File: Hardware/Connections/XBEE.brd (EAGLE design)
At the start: 34.3 x 28.9 mm, 3 parts

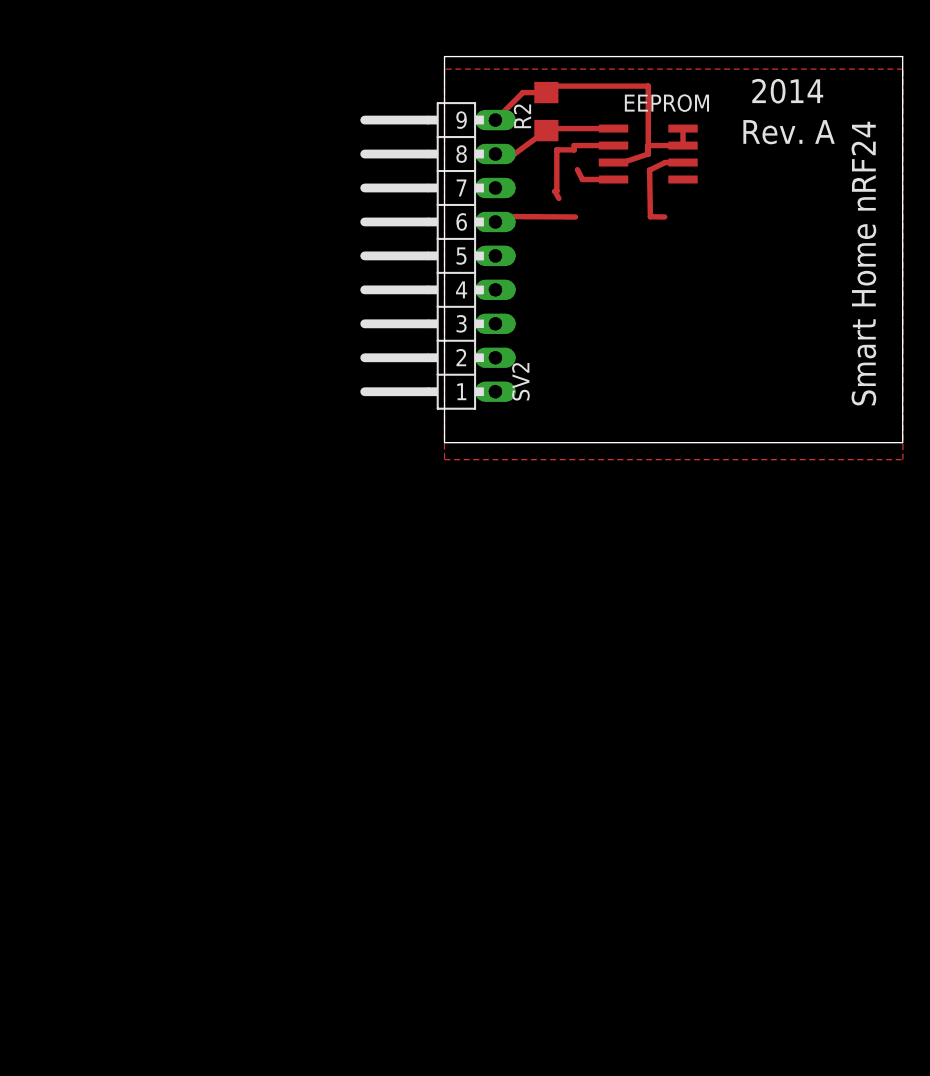
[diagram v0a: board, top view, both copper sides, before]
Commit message: updated XBEE Schematic. Added 3 Extra Pins for Serial protocol
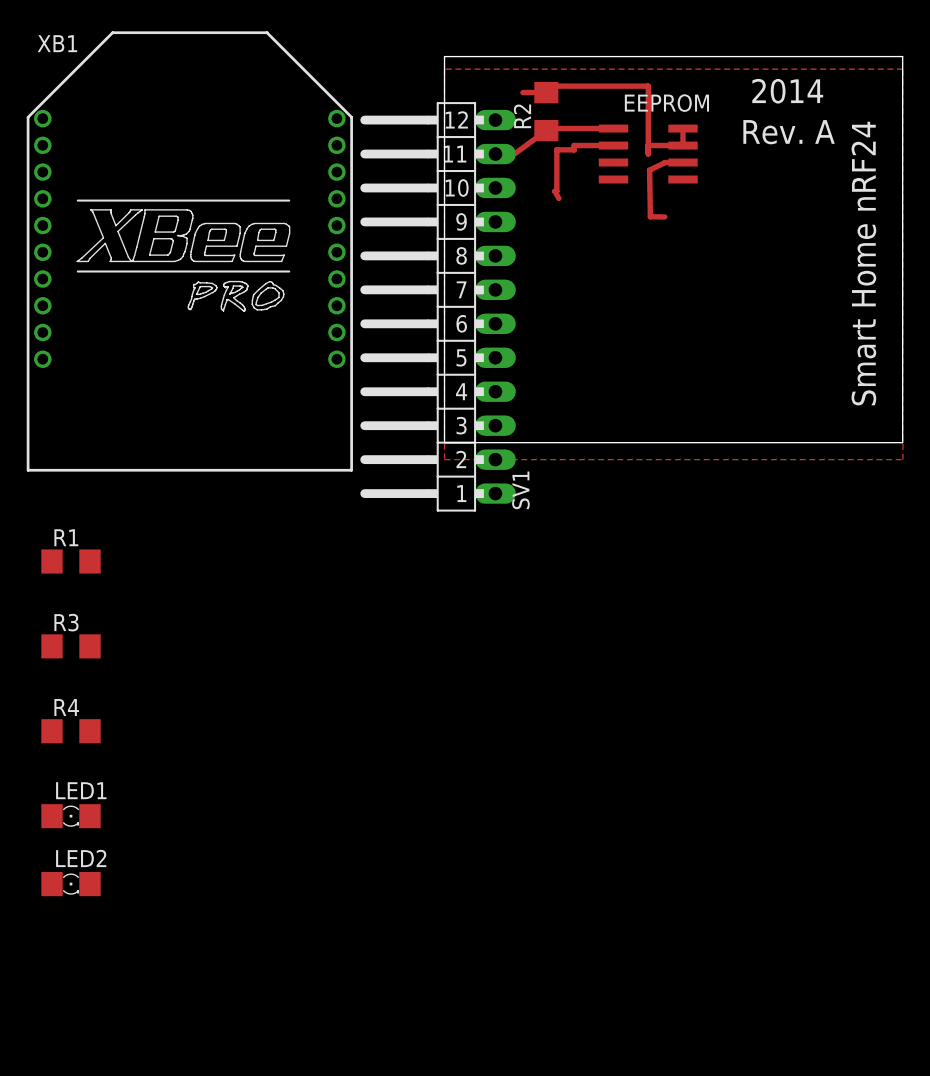
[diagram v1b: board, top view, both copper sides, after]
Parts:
- removed SV2: CON1, con-lstb:MA09-1W
- added LED1: ON_SLEEP, led:1206
- added LED2: Assoc, led:1206
- added R1, R3, R4: 10K, resistor:R1206
- added SV1: CON1, con-lstb:MA12-1W
- added XB1: XBEE-PRO, maxstream:XBEE-PRO
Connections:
- removed net N$4: EEPROM.4
- new net N$1: R1.2, XB1.5
- new net N$3: R4.2, XB1.13
- new net N$5: R3.2, XB1.15
- new net N$6: LED1.A, R4.1
- new net N$7: LED2.A, R3.1
- new net UART_RX: SV1.3, XB1.3
- new net UART_TX: SV1.2, XB1.2
- net +3V3: now also R1.1, SV1.12, XB1.1; no longer SV2.9
- net CE_RAD: now also SV1.5; no longer SV2.2
- net CSN_MEM: now also SV1.11; no longer SV2.8
- net CSN_RAD: now also SV1.6; no longer SV2.3
- net GND: now also EEPROM.4, LED1.C, LED2.C, SV1.4, XB1.10, XB1.14; no longer SV2.1
- net IRQ_RAD: now also SV1.8; no longer SV2.5
- net MISO: now also SV1.10; no longer SV2.7
- net MOSI: now also SV1.7; no longer SV2.4
- net SCK: now also SV1.9; no longer SV2.6
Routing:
- net SCK: track 13.2 -> 7.19 mm
- net +3V3: track 24.8 -> 19.2 mm
- net N$4: track 3.15 -> 0.00 mm
- net CSN_MEM: track 9.42 -> 8.00 mm
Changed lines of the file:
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@@
 </autorouter>
 <elements>
-<element name="SV2" library="con-lstb" package="MA09-1W" value="CON1" x="3.81" y="13.97" rot="R90">
-<attribute name="OC_NEWARK" value="unknown" x="25.4" y="39.37" size="1.778" layer="27" rot="R90" display="off"/>
-<attribute name="MPN" value="" x="25.4" y="39.37" size="1.778" layer="27" rot="R90" display="off"/>
-<attribute name="MF" value="" x="25.4" y="39.37" size="1.778" layer="27" rot="R90" display="off"/>
-<attribute name="OC_FARNELL" value="unknown" x="25.4" y="39.37" size="1.778" layer="27" rot="R90" display="off"/>
-</element>
 <element name="EEPROM" library="eeprom" package="SO8" value="BR25S640FJ-WE2" x="15.24" y="21.59" rot="R270"/>
 <element name="R2" library="resistor" package="R1206" value="10K" x="7.62" y="24.765" rot="R90"/>
+<element name="SV1" library="con-lstb" package="MA12-1W" value="CON1" x="3.81" y="10.16" rot="R90">
+<attribute name="OC_NEWARK" value="unknown" x="3.81" y="10.16" size="1.778" layer="27" rot="R90" display="off"/>
+<attribute name="MPN" value="" x="3.81" y="10.16" size="1.778" layer="27" rot="R90" display="off"/>
+<attribute name="MF" value="" x="3.81" y="10.16" size="1.778" layer="27" rot="R90" display="off"/>
+<attribute name="OC_FARNELL" value="unknown" x="3.81" y="10.16" size="1.778" layer="27" rot="R90" display="off"/>
+</element>
+<element name="XB1" library="maxstream" package="XBEE-PRO" value="XBEE-PRO" x="-19.05" y="15.24">
+<attribute name="OC_NEWARK" value="42M2667" x="-19.05" y="15.24" size="1.778" layer="27" display="off"/>
+<attribute name="MPN" value="XBP24-AWI-001" x="-19.05" y="15.24" size="1.778" layer="27" display="off"/>
+<attribute name="MF" value="" x="-19.05" y="15.24" size="1.778" layer="27" display="off"/>
+<attribute name="OC_FARNELL" value="1337916" x="-19.05" y="15.24" size="1.778" layer="27" display="off"/>
+</element>
+<element name="R1" library="resistor" package="R1206" value="10K" x="-27.94" y="-8.89"/>
+<element name="R3" library="resistor" package="R1206" value="10K" x="-27.94" y="-15.24"/>
+<element name="R4" library="resistor" package="R1206" value="10K" x="-27.94" y="-21.59"/>
+<element name="LED1" library="led" package="1206" value="ON_SLEEP" x="-27.94" y="-27.94"/>
+<element name="LED2" library="led" package="1206" value="Assoc" x="-27.94" y="-33.02"/>
 </elements>
 <signals>
 <signal name="+3V3">
-<contactref element="SV2" pad="9"/>
 <contactref element="EEPROM" pad="8"/>
 <contactref element="EEPROM" pad="7"/>
-<contactref element="EEPROM" pad="3"/>
 <contactref element="R2" pad="2"/>
 <wire x1="17.84" y1="23.495" x2="17.84" y2="22.225" width="0.4064" layer="1"/>
 <wire x1="7.62" y1="26.187" x2="5.867" y2="26.187" width="0.4064" layer="1"/>
-<wire x1="5.867" y1="26.187" x2="3.81" y2="24.13" width="0.4064" layer="1"/>
 <wire x1="17.84" y1="22.225" x2="15.205" y2="22.225" width="0.4064" layer="1"/>
 <wire x1="15.205" y1="22.225" x2="15.24" y2="21.59" width="0.4064" layer="1"/>
-<wire x1="15.24" y1="21.59" x2="13.335" y2="20.955" width="0.4064" layer="1"/>
-<wire x1="13.335" y1="20.955" x2="12.64" y2="20.955" width="0.4064" layer="1"/>
 <wire x1="7.62" y1="26.187" x2="8.103" y2="26.67" width="0.4064" layer="1"/>
 <wire x1="8.103" y1="26.67" x2="15.24" y2="26.67" width="0.4064" layer="1"/>
 <wire x1="15.24" y1="26.67" x2="15.24" y2="21.59" width="0.4064" layer="1"/>
+<contactref element="EEPROM" pad="3"/>
+<contactref element="SV1" pad="12"/>
+<contactref element="XB1" pad="1"/>
+<contactref element="R1" pad="1"/>
+<wire x1="-30.05" y1="24.24" x2="-29.362" y2="-8.89" width="0" layer="19" extent="1-1"/>
+<wire x1="3.81" y1="24.13" x2="-30.05" y2="24.24" width="0" layer="19" extent="1-1"/>
+<wire x1="5.867" y1="26.187" x2="3.81" y2="24.13" width="0" layer="19" extent="1-1"/>
+<wire x1="12.64" y1="20.955" x2="15.24" y2="21.59" width="0" layer="19" extent="1-1"/>
 </signal>
 <signal name="GND">
-<contactref element="SV2" pad="1"/>
 <polygon width="0.4064" layer="1" isolate="0.4064">
 <vertex x="0" y="27.94"/>
@@
 <vertex x="34.29" y="27.94"/>
 </polygon>
+<contactref element="EEPROM" pad="4"/>
+<contactref element="SV1" pad="4"/>
+<contactref element="XB1" pad="10"/>
+<contactref element="XB1" pad="10"/>
+<contactref element="XB1" pad="14"/>
+<contactref element="LED2" pad="C"/>
+<contactref element="LED1" pad="C"/>
+<wire x1="-26.518" y1="-27.94" x2="-26.518" y2="-33.02" width="0" layer="19" extent="1-1"/>
+<wire x1="-30.05" y1="6.24" x2="-26.518" y2="-27.94" width="0" layer="19" extent="1-1"/>
+<wire x1="-8.05" y1="12.24" x2="-30.05" y2="6.24" width="0" layer="19" extent="1-1"/>
+<wire x1="3.81" y1="3.81" x2="-8.05" y2="12.24" width="0" layer="19" extent="1-1"/>
+<wire x1="12.64" y1="19.685" x2="3.81" y2="3.81" width="0" layer="19" extent="1-1"/>
 </signal>
 <signal name="MISO">
 <contactref element="EEPROM" pad="2"/>
-<contactref element="SV2" pad="7"/>
 <wire x1="12.64" y1="22.225" x2="9.7" y2="22.225" width="0.4064" layer="1"/>
 <wire x1="9.7" y1="22.225" x2="9.7" y2="21.9" width="0.4064" layer="1"/>
@@
 <wire x1="8.4" y1="18.8" x2="8.255" y2="18.8" width="0.4064" layer="1"/>
 <wire x1="8.255" y1="18.8" x2="8.555" y2="18.267" width="0.4064" layer="1"/>
-<wire x1="3.81" y1="18.8" x2="3.81" y2="19.05" width="0.4064" layer="1"/>
+<contactref element="SV1" pad="10"/>
 <wire x1="3.81" y1="19.05" x2="8.255" y2="18.8" width="0" layer="19" extent="1-1"/>
 </signal>
 <signal name="MOSI">
 <contactref element="EEPROM" pad="5"/>
-<contactref element="SV2" pad="4"/>
+<contactref element="SV1" pad="7"/>
 <wire x1="3.81" y1="11.43" x2="17.84" y2="19.685" width="0" layer="19" extent="1-1"/>
 </signal>
@@
 <wire x1="15.34" y1="20.385" x2="16.51" y2="20.955" width="0.4064" layer="1"/>
 <wire x1="16.51" y1="20.955" x2="17.84" y2="20.955" width="0.4064" layer="1"/>
-<wire x1="9.79" y1="16.88" x2="5.12" y2="16.91" width="0.4064" layer="1"/>
-<contactref element="SV2" pad="6"/>
-<wire x1="5.12" y1="16.91" x2="3.81" y2="16.51" width="0.4064" layer="1"/>
-<wire x1="9.79" y1="16.88" x2="15.4" y2="16.9" width="0" layer="19" extent="1-1"/>
-</signal>
-<signal name="CSN_RAD">
-<contactref element="SV2" pad="3"/>
-</signal>
-<signal name="CE_RAD">
-<contactref element="SV2" pad="2"/>
+<contactref element="SV1" pad="9"/>
+<wire x1="3.81" y1="16.51" x2="15.4" y2="16.9" width="0" layer="19" extent="1-1"/>
 </signal>
 <signal name="CSN_MEM">
 <contactref element="R2" pad="1"/>
 <contactref element="EEPROM" pad="1"/>
-<contactref element="SV2" pad="8"/>
 <wire x1="12.64" y1="23.495" x2="8.407" y2="23.495" width="0.4064" layer="1"/>
 <wire x1="8.407" y1="23.495" x2="7.62" y2="23.343" width="0.4064" layer="1"/>
 <wire x1="7.62" y1="23.343" x2="5.232" y2="21.59" width="0.4064" layer="1"/>
-<wire x1="5.232" y1="21.59" x2="3.81" y2="21.59" width="0.4064" layer="1"/>
-</signal>
-<signal name="IRQ_RAD">
-<contactref element="SV2" pad="5"/>
+<contactref element="SV1" pad="11"/>
+<wire x1="3.81" y1="21.59" x2="5.232" y2="21.59" width="0" layer="19" extent="1-1"/>
 </signal>
 <signal name="N$2">
 </signal>
 <signal name="N$4">
-<contactref element="EEPROM" pad="4"/>
-<wire x1="12.64" y1="19.685" x2="10.312" y2="19.685" width="0.4064" layer="1"/>
-<wire x1="10.312" y1="19.685" x2="9.942" y2="20.42" width="0.4064" layer="1"/>
+</signal>
+<signal name="CSN_RAD">
+<contactref element="SV1" pad="6"/>
+</signal>
+<signal name="CE_RAD">
+<contactref element="SV1" pad="5"/>
+</signal>
+<signal name="IRQ_RAD">
+<contactref element="SV1" pad="8"/>
+</signal>
+<signal name="UART_RX">
+<contactref element="SV1" pad="3"/>
+<contactref element="XB1" pad="3"/>
+<wire x1="3.81" y1="1.27" x2="-30.05" y2="20.24" width="0" layer="19" extent="1-1"/>
+</signal>
+<signal name="UART_TX">
+<contactref element="SV1" pad="2"/>
+<contactref element="XB1" pad="2"/>
+<wire x1="3.81" y1="-1.27" x2="-30.05" y2="22.24" width="0" layer="19" extent="1-1"/>
+</signal>
+<signal name="N$1">
+<contactref element="XB1" pad="5"/>
+<contactref element="R1" pad="2"/>
+<wire x1="-30.05" y1="16.24" x2="-26.518" y2="-8.89" width="0" layer="19" extent="1-1"/>
+</signal>
+<signal name="N$3">
+<contactref element="XB1" pad="13"/>
+<contactref element="R4" pad="2"/>
+<wire x1="-8.05" y1="10.24" x2="-26.518" y2="-21.59" width="0" layer="19" extent="1-1"/>
+</signal>
+<signal name="N$5">
+<contactref element="XB1" pad="15"/>
+<contactref element="R3" pad="2"/>
+<wire x1="-8.05" y1="14.24" x2="-26.518" y2="-15.24" width="0" layer="19" extent="1-1"/>
+</signal>
+<signal name="N$6">
+<contactref element="R4" pad="1"/>
+<contactref element="LED1" pad="A"/>
+<wire x1="-29.362" y1="-21.59" x2="-29.362" y2="-27.94" width="0" layer="19" extent="1-1"/>
+</signal>
+<signal name="N$7">
+<contactref element="R3" pad="1"/>
+<contactref element="LED2" pad="A"/>
+<wire x1="-29.362" y1="-15.24" x2="-29.362" y2="-33.02" width="0" layer="19" extent="1-1"/>
 </signal>
 </signals>

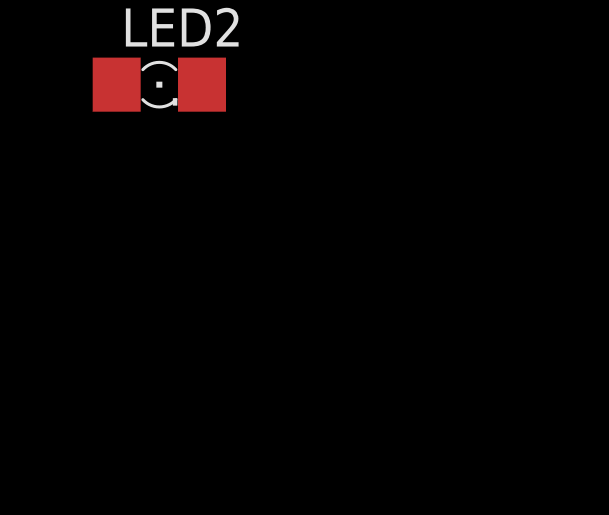
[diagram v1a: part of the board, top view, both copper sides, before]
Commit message: added missing components to XBEE schematic
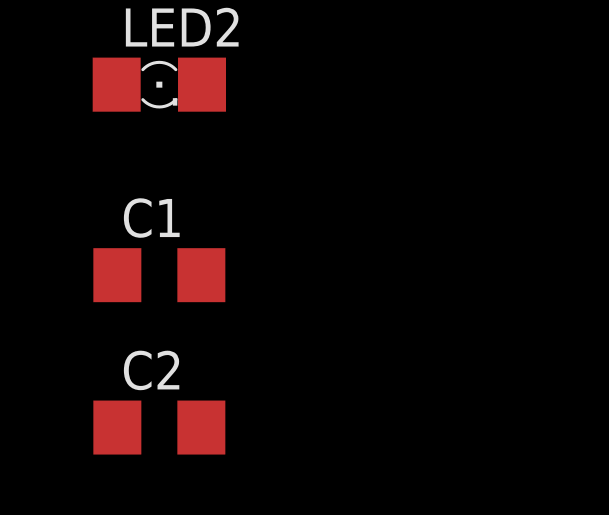
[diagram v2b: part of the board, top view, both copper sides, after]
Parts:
- added C1: 8.2p, rcl:C1206
- added C2: 1u, rcl:C1206
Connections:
- net +3V3: now also C1.1, C2.1
- net GND: now also C1.2, C2.2
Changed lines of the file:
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@@
 <element name="LED1" library="led" package="1206" value="ON_SLEEP" x="-27.94" y="-27.94"/>
 <element name="LED2" library="led" package="1206" value="Assoc" x="-27.94" y="-33.02"/>
+<element name="C1" library="rcl" package="C1206" value="8.2p" x="-27.94" y="-39.37"/>
+<element name="C2" library="rcl" package="C1206" value="1u" x="-27.94" y="-44.45"/>
 </elements>
 <signals>
@@
 <contactref element="XB1" pad="1"/>
 <contactref element="R1" pad="1"/>
+<contactref element="C2" pad="1"/>
+<contactref element="C1" pad="1"/>
+<wire x1="-29.34" y1="-39.37" x2="-29.34" y2="-44.45" width="0" layer="19" extent="1-1"/>
+<wire x1="-29.362" y1="-8.89" x2="-29.34" y2="-39.37" width="0" layer="19" extent="1-1"/>
 <wire x1="-30.05" y1="24.24" x2="-29.362" y2="-8.89" width="0" layer="19" extent="1-1"/>
 <wire x1="3.81" y1="24.13" x2="-30.05" y2="24.24" width="0" layer="19" extent="1-1"/>
@@
 <contactref element="LED2" pad="C"/>
 <contactref element="LED1" pad="C"/>
+<contactref element="C1" pad="2"/>
+<contactref element="C2" pad="2"/>
+<wire x1="-26.54" y1="-39.37" x2="-26.54" y2="-44.45" width="0" layer="19" extent="1-1"/>
+<wire x1="-26.518" y1="-33.02" x2="-26.54" y2="-39.37" width="0" layer="19" extent="1-1"/>
 <wire x1="-26.518" y1="-27.94" x2="-26.518" y2="-33.02" width="0" layer="19" extent="1-1"/>
 <wire x1="-30.05" y1="6.24" x2="-26.518" y2="-27.94" width="0" layer="19" extent="1-1"/>
